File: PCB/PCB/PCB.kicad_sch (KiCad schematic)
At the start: 8 parts, among them Q1 2N3905, Q2 2N3905, U1 ESP32-S3, U2 CP2104

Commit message: first PCB draft
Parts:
- removed Q1, Q2: 2N3905, Package_TO_SOT_THT:TO-92_Inline, symbol Transistor_BJT:2N3905
- removed U1: ESP32-S3, Package_DFN_QFN:QFN-56-1EP_7x7mm_P0.4mm_EP5.6x5.6mm, symbol Espressif:ESP32-S3
- removed U2: CP2104, Package_DFN_QFN:QFN-24-1EP_4x4mm_P0.5mm_EP2.6x2.6mm, symbol Interface_USB:CP2104
- added C1, C5: 1u, symbol Device:C
- added C2, C3, C4: 10u, symbol Device:C
- added D1, D2, D3: D_TVS, Diode_SMD:D_0603_1608Metric, symbol Device:D_TVS
- added D4: SS34FA, Diode_SMD:D_SOD-123F, symbol Diode:MBR1020VL
- added J2: USB_B_Micro, Connector_USB:USB_Micro-B_Molex-105017-0001, symbol Connector:USB_B_Micro
- added Q1, Q2: BC817, Package_TO_SOT_SMD:SOT-23, symbol Transistor_BJT:BC817
- added Q3: BSS84, Package_TO_SOT_SMD:SOT-23, symbol Transistor_FET:BSS84
- added R5, R8: 10K, symbol Device:R
- added R6, R7: R, symbol Device:R
- added U1: ESP32-S3-WROOM-1, Espressif:ESP32-S3-WROOM-1, symbol Espressif:ESP32-S3-WROOM-1
- added U2: CP2102N-Axx-xQFN28, Package_DFN_QFN:QFN-28-1EP_5x5mm_P0.5mm_EP3.35x3.35mm, symbol Interface_USB:CP2102N-Axx-xQFN28
- added U3: NCP1117-3.3_SOT223, Package_TO_SOT_SMD:SOT-223-3_TabPin2, symbol Regulator_Linear:NCP1117-3.3_SOT223
- R1: value R -> 47K
- R2: value R -> 22K
- R3: value R -> 1K
- R4: value R -> 10K
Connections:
- net at R2.1: now also R1.1, C1.2, U2.8 (VBUS)
- net at R2.2: now also D3.1 (A1), J2.1 (VBUS)
- net at R4.1: now also U2.24 (~{RTS})
- net at R4.2: now also Q1.1 (B)
- net +3.3V: now reaches R3.1
- net +3.3V: now also C2.1, C4.1, C5.1, U1.2 (3V3), U2.6 (VDD), U2.7 (VREGIN), U3.2 (VO)
- net at R3.2: now also U2.9 (~{RST})
- net GND: now reaches R1.2
- net GND: now also C1.1, C2.2, C3.2, C4.2, C5.2, D1.2 (A2), D2.2 (A2), D3.2 (A2), J2.5 (GND), J2.6 (Shield), R8.2, U1.1 (GND), U1.40 (GND), U1.41 (GND), U2.29 (GND), U2.3 (GND), U3.1 (GND)
- new net: Q1.3 (C), R6.1
- new net: D1.1 (A1), J2.2 (D-), U2.5 (D-)
- new net: D2.1 (A1), J2.3 (D+), U2.4 (D+)
- new net: Q2.1 (B), R5.2
- new net: Q2.3 (C), R7.1
- new net: R5.1, U2.28 (~{DTR})
- new net: C3.1, D4.1 (K), Q3.2 (S), U3.3 (VI)
- new net +BATT: Q3.3 (D)
- new net EN: R7.2, U1.3 (EN)
- new net GPIO0: R6.2
- new net VBUS: D4.2 (A), Q3.1 (G), R8.1
- new net rxd: U2.25 (RXD)
- new net txd: U2.26 (TXD)
- no-connect marks 0 -> 9
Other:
- moved on the sheet: R1, R2, R3, R4

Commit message: first draft
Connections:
- net GPIO0: now also U1.27 (GPIO0/BOOT)
- net rxd: now also U1.36 (U0RXD/GPIO44/CLK_OUT2)
- net txd: now also U1.37 (U0TXD/GPIO43/CLK_OUT1)
- net at Q1.2 (E): now also R5.1, U2.28 (~{DTR})
- net at Q2.2 (E): now also R4.1, U2.24 (~{RTS})
- no-connect marks 9 -> 13
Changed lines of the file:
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@@
 (kicad_sch (version 20230121) (generator eeschema)
-  (paper "A4")
+  (paper "A3")
   (junction (at 36.83 88.9) (diameter 0) (color 0 0 0 0)
   )
@@
   (junction (at 76.2 57.15) (diameter 0) (color 0 0 0 0)
   )
+  (junction (at 88.9 93.98) (diameter 0) (color 0 0 0 0)
+  )
   (junction (at 59.69 29.21) (diameter 0) (color 0 0 0 0)
   )
@@
   )
   (junction (at 22.86 24.13) (diameter 0) (color 0 0 0 0)
+  )
+  (junction (at 86.36 88.9) (diameter 0) (color 0 0 0 0)
   )
   (junction (at 35.56 96.52) (diameter 0) (color 0 0 0 0)
@@
   (no_connect (at 83.82 111.76))
   (no_connect (at 83.82 116.84))
+  (no_connect (at 83.82 93.98))
   (no_connect (at 83.82 121.92))
   (no_connect (at 83.82 106.68))
   (no_connect (at 83.82 101.6))
+  (no_connect (at 83.82 83.82))
+  (no_connect (at 83.82 86.36))
+  (no_connect (at 83.82 91.44))
   (no_connect (at 83.82 114.3))
   (no_connect (at 83.82 109.22))
@@
     (stroke (width 0) (type default))
   )
+  (wire (pts (xy 242.57 63.5) (xy 236.22 63.5))
+    (stroke (width 0) (type default))
+  )
+  (wire (pts (xy 86.36 88.9) (xy 90.17 88.9))
+    (stroke (width 0) (type default))
+  )
   (wire (pts (xy 50.8 91.44) (xy 58.42 91.44))
     (stroke (width 0) (type default))
@@
     (stroke (width 0) (type default))
   )
-  (wire (pts (xy 83.82 88.9) (xy 90.17 88.9))
+  (wire (pts (xy 83.82 88.9) (xy 86.36 88.9))
     (stroke (width 0) (type default))
   )
@@
     (stroke (width 0) (type default))
   )
+  (wire (pts (xy 270.51 76.2) (xy 236.22 76.2))
+    (stroke (width 0) (type default))
+  )
   (wire (pts (xy 35.56 116.84) (xy 41.91 116.84))
     (stroke (width 0) (type default))
@@
     (stroke (width 0) (type default))
   )
+  (wire (pts (xy 114.3 49.53) (xy 114.3 76.2))
+    (stroke (width 0) (type default))
+  )
+  (wire (pts (xy 240.03 49.53) (xy 114.3 49.53))
+    (stroke (width 0) (type default))
+  )
+  (wire (pts (xy 114.3 76.2) (xy 83.82 76.2))
+    (stroke (width 0) (type default))
+  )
+  (wire (pts (xy 88.9 93.98) (xy 105.41 93.98))
+    (stroke (width 0) (type default))
+  )
   (wire (pts (xy 33.02 88.9) (xy 36.83 88.9))
     (stroke (width 0) (type default))
@@
     (stroke (width 0) (type default))
   )
+  (wire (pts (xy 236.22 60.96) (xy 240.03 60.96))
+    (stroke (width 0) (type default))
+  )
   (wire (pts (xy 116.84 83.82) (xy 116.84 60.96))
     (stroke (width 0) (type default))
   )
+  (wire (pts (xy 116.84 107.95) (xy 116.84 156.21))
+    (stroke (width 0) (type default))
+  )
   (wire (pts (xy 41.91 116.84) (xy 46.99 116.84))
     (stroke (width 0) (type default))
   )
+  (wire (pts (xy 116.84 156.21) (xy 270.51 156.21))
+    (stroke (width 0) (type default))
+  )
   (wire (pts (xy 22.86 24.13) (xy 22.86 29.21))
     (stroke (width 0) (type default))
   )
+  (wire (pts (xy 111.76 46.99) (xy 242.57 46.99))
+    (stroke (width 0) (type default))
+  )
   (wire (pts (xy 35.56 106.68) (xy 35.56 116.84))
     (stroke (width 0) (type default))
@@
     (stroke (width 0) (type default))
   )
+  (wire (pts (xy 270.51 156.21) (xy 270.51 76.2))
+    (stroke (width 0) (type default))
+  )
   (wire (pts (xy 113.03 83.82) (xy 116.84 83.82))
     (stroke (width 0) (type default))
@@
     (stroke (width 0) (type default))
   )
+  (wire (pts (xy 242.57 46.99) (xy 242.57 63.5))
+    (stroke (width 0) (type default))
+  )
+  (wire (pts (xy 105.41 97.79) (xy 86.36 97.79))
+    (stroke (width 0) (type default))
+  )
   (wire (pts (xy 46.99 73.66) (xy 50.8 73.66))
     (stroke (width 0) (type default))
   )
-  (wire (pts (xy 88.9 102.87) (xy 88.9 81.28))
+  (wire (pts (xy 88.9 102.87) (xy 88.9 93.98))
     (stroke (width 0) (type default))
   )
@@
     (stroke (width 0) (type default))
   )
+  (wire (pts (xy 111.76 78.74) (xy 111.76 46.99))
+    (stroke (width 0) (type default))
+  )
   (wire (pts (xy 68.58 71.12) (xy 71.12 71.12))
     (stroke (width 0) (type default))
   )
+  (wire (pts (xy 83.82 78.74) (xy 111.76 78.74))
+    (stroke (width 0) (type default))
+  )
   (wire (pts (xy 33.02 93.98) (xy 41.91 93.98))
     (stroke (width 0) (type default))
   )
+  (wire (pts (xy 88.9 93.98) (xy 88.9 81.28))
+    (stroke (width 0) (type default))
+  )
   (wire (pts (xy 22.86 104.14) (xy 24.13 104.14))
     (stroke (width 0) (type default))
   )
+  (wire (pts (xy 240.03 60.96) (xy 240.03 49.53))
+    (stroke (width 0) (type default))
+  )
+  (wire (pts (xy 113.03 107.95) (xy 116.84 107.95))
+    (stroke (width 0) (type default))
+  )
   (wire (pts (xy 35.56 96.52) (xy 35.56 99.06))
     (stroke (width 0) (type default))
@@
     (stroke (width 0) (type default))
   )
-  (label "txd" (at 207.01 57.15 0) (fields_autoplaced)
+  (wire (pts (xy 86.36 97.79) (xy 86.36 88.9))
+    (stroke (width 0) (type default))
+  )
+  (label "txd" (at 236.22 60.96 0) (fields_autoplaced)
     (effects (font (size 1.27 1.27)) (justify left bottom))
   )
@@
     (effects (font (size 1.27 1.27)) (justify left bottom))
   )
-  (label "rxd" (at 207.01 59.69 0) (fields_autoplaced)
+  (label "rxd" (at 236.22 63.5 0) (fields_autoplaced)
     (effects (font (size 1.27 1.27)) (justify left bottom))
   )
@@
   )
   (symbol (lib_id "Device:R") (at 109.22 83.82 90) (unit 1)
-    (in_bom yes) (on_board yes) (dnp no) (fields_autoplaced)
-    (property "Reference" "R7" (at 109.22 78.74 90)
-      (effects (font (size 1.27 1.27)))
-    )
-    (property "Value" "R" (at 109.22 81.28 90)
-      (effects (font (size 1.27 1.27)))
-    )
+    (in_bom yes) (on_board yes) (dnp no)
+    (property "Reference" "R7" (at 105.41 80.01 90)
+      (effects (font (size 1.27 1.27)))
+    )
+    (property "Value" "R" (at 105.41 82.55 90)
+      (effects (font (size 1.27 1.27)))
+    )

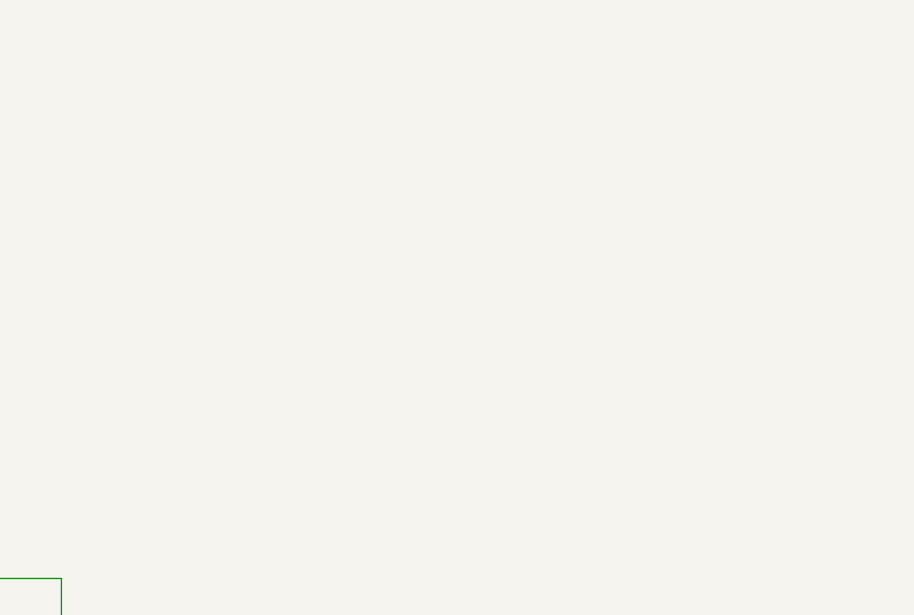
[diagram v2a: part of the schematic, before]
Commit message: added DAC and AMP
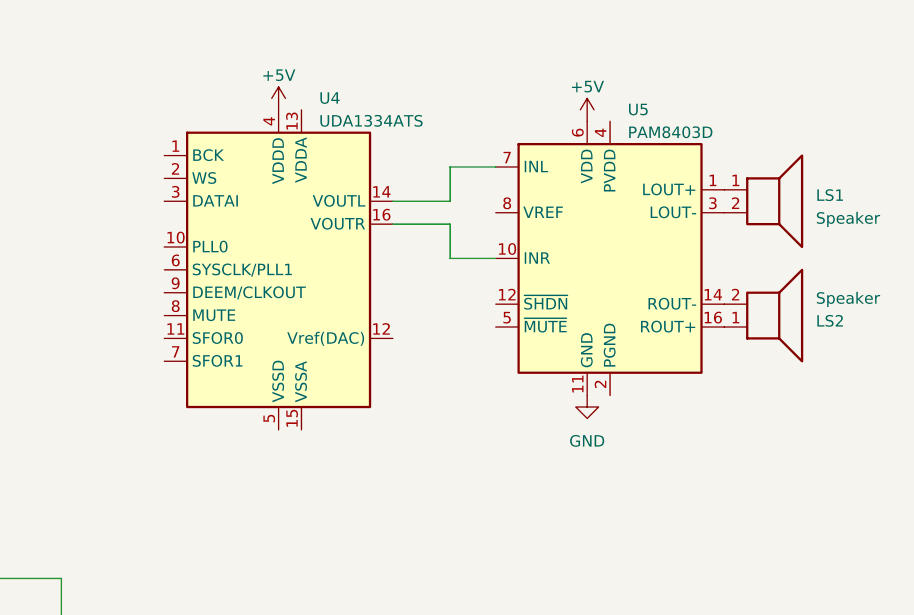
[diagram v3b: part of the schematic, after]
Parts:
- added LS1, LS2: Speaker, symbol Device:Speaker
- added U4: UDA1334ATS, Package_SO:SSOP-16_4.4x5.2mm_P0.65mm, symbol Audio:UDA1334ATS
- added U5: PAM8403D, Package_SO:SOP-16_3.9x9.9mm_P1.27mm, symbol Amplifier_Audio:PAM8403D
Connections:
- net GND: now also U5.11 (GND)
- new net: LS1.1, U5.1 (LOUT+)
- new net: U4.16 (VOUTR), U5.10 (INR)
- new net: U5.13 (PVDD), U5.4 (PVDD)
- new net: LS2.2, U5.14 (ROUT-)
- new net: U5.15 (PGND), U5.2 (PGND)
- new net: LS2.1, U5.16 (ROUT+)
- new net: LS1.2, U5.3 (LOUT-)
- new net: U4.14 (VOUTL), U5.7 (INL)
- new net +5V: U4.4 (VDDD), U5.6 (VDD)
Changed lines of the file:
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@@
+    (stroke (width 0) (type default))
+  )
+  (wire (pts (xy 307.34 34.29) (xy 313.69 34.29))
     (stroke (width 0) (type default))
   )
@@
     (stroke (width 0) (type default))
   )
+  (wire (pts (xy 313.69 34.29) (xy 313.69 30.48))
+    (stroke (width 0) (type default))
+  )
   (wire (pts (xy 71.12 71.12) (xy 71.12 57.15))
     (stroke (width 0) (type default))
@@
     (stroke (width 0) (type default))
   )
+  (wire (pts (xy 307.34 36.83) (xy 313.69 36.83))
+    (stroke (width 0) (type default))
+  )
   (wire (pts (xy 58.42 81.28) (xy 58.42 88.9))
     (stroke (width 0) (type default))
   )
+  (wire (pts (xy 313.69 30.48) (xy 318.77 30.48))
+    (stroke (width 0) (type default))
+  )
   (wire (pts (xy 36.83 88.9) (xy 46.99 88.9))
     (stroke (width 0) (type default))
@@
     (stroke (width 0) (type default))
   )
+  (wire (pts (xy 313.69 36.83) (xy 313.69 40.64))
+    (stroke (width 0) (type default))
+  )
   (wire (pts (xy 22.86 24.13) (xy 22.86 29.21))
     (stroke (width 0) (type default))
@@
   )
   (wire (pts (xy 105.41 97.79) (xy 86.36 97.79))
+    (stroke (width 0) (type default))
+  )
+  (wire (pts (xy 313.69 40.64) (xy 318.77 40.64))
     (stroke (width 0) (type default))
   )
@@
   (label "rxd" (at 236.22 63.5 0) (fields_autoplaced)
     (effects (font (size 1.27 1.27)) (justify left bottom))
+  )
+  (symbol (lib_id "power:+5V") (at 294.64 24.13 0) (unit 1)
+    (in_bom yes) (on_board yes) (dnp no) (fields_autoplaced)
+    (property "Reference" "#PWR019" (at 294.64 27.94 0)
+      (effects (font (size 1.27 1.27)) hide)
+    )
+    (property "Value" "+5V" (at 294.64 20.32 0)
+      (effects (font (size 1.27 1.27)))
+    )
+    (property "Footprint" "" (at 294.64 24.13 0)
+      (effects (font (size 1.27 1.27)) hide)
+    )
+    (property "Datasheet" "" (at 294.64 24.13 0)
+      (effects (font (size 1.27 1.27)) hide)
+    )
+    (pin "1")
+    (instances
+      (project "PCB"
+        (path "/8a45fe01-405d-4f4d-910d-01ae941f9b06"
+          (reference "#PWR019") (unit 1)
+        )
+      )
+    )
   )
   (symbol (lib_id "power:+3.3V") (at 190.5 55.88 0) (unit 1)
@@
         (path "/8a45fe01-405d-4f4d-910d-01ae941f9b06"
           (reference "#PWR01") (unit 1)
+        )
+      )
+    )
+  )
+  (symbol (lib_id "power:GND") (at 328.93 55.88 0) (unit 1)
+    (in_bom yes) (on_board yes) (dnp no) (fields_autoplaced)
+    (property "Reference" "#PWR018" (at 328.93 62.23 0)
+      (effects (font (size 1.27 1.27)) hide)
+    )
+    (property "Value" "GND" (at 328.93 60.96 0)
+      (effects (font (size 1.27 1.27)))
+    )
+    (property "Footprint" "" (at 328.93 55.88 0)
+      (effects (font (size 1.27 1.27)) hide)
+    )
+    (property "Datasheet" "" (at 328.93 55.88 0)
+      (effects (font (size 1.27 1.27)) hide)
+    )
+    (pin "1")
+    (instances
+      (project "PCB"
+        (path "/8a45fe01-405d-4f4d-910d-01ae941f9b06"
+          (reference "#PWR018") (unit 1)
         )
       )
@@
     )
   )
+  (symbol (lib_id "Amplifier_Audio:PAM8403D") (at 331.47 40.64 0) (unit 1)
+    (in_bom yes) (on_board yes) (dnp no) (fields_autoplaced)
+    (property "Reference" "U5" (at 333.4259 24.13 0)
+      (effects (font (size 1.27 1.27)) (justify left))
+    )
+    (property "Value" "PAM8403D" (at 333.4259 26.67 0)
+      (effects (font (size 1.27 1.27)) (justify left))
+    )
+    (property "Footprint" "Package_SO:SOP-16_3.9x9.9mm_P1.27mm" (at 331.47 40.64 0)
+      (effects (font (size 1.27 1.27)) hide)
+    )
+    (property "Datasheet" "https://www.diodes.com/assets/Datasheets/PAM8403.pdf" (at 326.39 35.56 0)
+      (effects (font (size 1.27 1.27)) hide)
+    )
+    (pin "1")
+    (pin "10")
+    (pin "11")
+    (pin "12")
+    (pin "13")
+    (pin "14")
+    (pin "15")
+    (pin "16")
+    (pin "2")
+    (pin "3")
+    (pin "4")
+    (pin "5")
+    (pin "6")
+    (pin "7")
+    (pin "8")
+    (pin "9")
+    (instances
+      (project "PCB"
+        (path "/8a45fe01-405d-4f4d-910d-01ae941f9b06"
+          (reference "U5") (unit 1)
+        )
+      )
+    )
+  )
   (symbol (lib_id "power:GND") (at 59.69 36.83 0) (unit 1)
     (in_bom yes) (on_board yes) (dnp no) (fields_autoplaced)
@@
     )
   )
+  (symbol (lib_id "Device:Speaker") (at 349.25 33.02 0) (unit 1)
+    (in_bom yes) (on_board yes) (dnp no) (fields_autoplaced)
+    (property "Reference" "LS1" (at 354.33 33.655 0)
+      (effects (font (size 1.27 1.27)) (justify left))
+    )
+    (property "Value" "Speaker" (at 354.33 36.195 0)
+      (effects (font (size 1.27 1.27)) (justify left))
+    )
+    (property "Footprint" "" (at 349.25 38.1 0)
+      (effects (font (size 1.27 1.27)) hide)
+    )
+    (property "Datasheet" "~" (at 348.996 34.29 0)
+      (effects (font (size 1.27 1.27)) hide)
+    )
+    (pin "1")
+    (pin "2")
+    (instances
+      (project "PCB"
+        (path "/8a45fe01-405d-4f4d-910d-01ae941f9b06"
+          (reference "LS1") (unit 1)
+        )
+      )
+    )
+  )
   (symbol (lib_id "power:GND") (at 190.5 137.16 0) (unit 1)
     (in_bom yes) (on_board yes) (dnp no) (fields_autoplaced)
@@
         (path "/8a45fe01-405d-4f4d-910d-01ae941f9b06"
           (reference "#PWR011") (unit 1)
+        )
+      )
+    )
+  )
+  (symbol (lib_id "Device:Speaker") (at 349.25 48.26 0) (mirror x) (unit 1)
+    (in_bom yes) (on_board yes) (dnp no)
+    (property "Reference" "LS2" (at 354.33 47.625 0)
+      (effects (font (size 1.27 1.27)) (justify left))
+    )
+    (property "Value" "Speaker" (at 354.33 45.085 0)
+      (effects (font (size 1.27 1.27)) (justify left))
+    )
+    (property "Footprint" "" (at 349.25 43.18 0)
+      (effects (font (size 1.27 1.27)) hide)
+    )
+    (property "Datasheet" "~" (at 348.996 46.99 0)
+      (effects (font (size 1.27 1.27)) hide)
+    )
+    (pin "1")
+    (pin "2")
+    (instances
+      (project "PCB"
+        (path "/8a45fe01-405d-4f4d-910d-01ae941f9b06"
+          (reference "LS2") (unit 1)
+        )
+      )
+    )
+  )
+  (symbol (lib_id "Audio:UDA1334ATS") (at 294.64 41.91 0) (unit 1)
+    (in_bom yes) (on_board yes) (dnp no) (fields_autoplaced)
+    (property "Reference" "U4" (at 299.1359 22.86 0)
+      (effects (font (size 1.27 1.27)) (justify left))
+    )
+    (property "Value" "UDA1334ATS" (at 299.1359 25.4 0)
+      (effects (font (size 1.27 1.27)) (justify left))
+    )
+    (property "Footprint" "Package_SO:SSOP-16_4.4x5.2mm_P0.65mm" (at 294.64 41.91 0)
+      (effects (font (size 1.27 1.27)) hide)
+    )
+    (property "Datasheet" "http://www.nxp.com/docs/en/data-sheet/UDA1334ATS.pdf" (at 294.64 41.91 0)
+      (effects (font (size 1.27 1.27)) hide)
+    )
+    (pin "1")
+    (pin "10")
+    (pin "11")
+    (pin "12")
+    (pin "13")
+    (pin "14")
+    (pin "15")
+    (pin "16")
+    (pin "2")
+    (pin "3")
+    (pin "4")
+    (pin "5")
+    (pin "6")
+    (pin "7")
+    (pin "8")
+    (pin "9")
+    (instances
+      (project "PCB"
+        (path "/8a45fe01-405d-4f4d-910d-01ae941f9b06"
+          (reference "U4") (unit 1)
         )
       )
@@
         )
       )
+    )
+  )
+  (symbol (lib_id "power:+5V") (at 328.93 25.4 0) (unit 1)
+    (in_bom yes) (on_board yes) (dnp no) (fields_autoplaced)
+    (property "Reference" "#PWR020" (at 328.93 29.21 0)
+      (effects (font (size 1.27 1.27)) hide)
+    )
+    (property "Value" "+5V" (at 328.93 21.59 0)
+      (effects (font (size 1.27 1.27)))
+    )
+    (property "Footprint" "" (at 328.93 25.4 0)
+      (effects (font (size 1.27 1.27)) hide)
+    )
+    (property "Datasheet" "" (at 328.93 25.4 0)
+      (effects (font (size 1.27 1.27)) hide)
+    )
+    (pin "1")
+    (instances
+      (project "PCB"
+        (path "/8a45fe01-405d-4f4d-910d-01ae941f9b06"
+          (reference "#PWR020") (unit 1)
+        )
+      )
